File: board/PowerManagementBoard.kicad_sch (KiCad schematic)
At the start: 0 parts

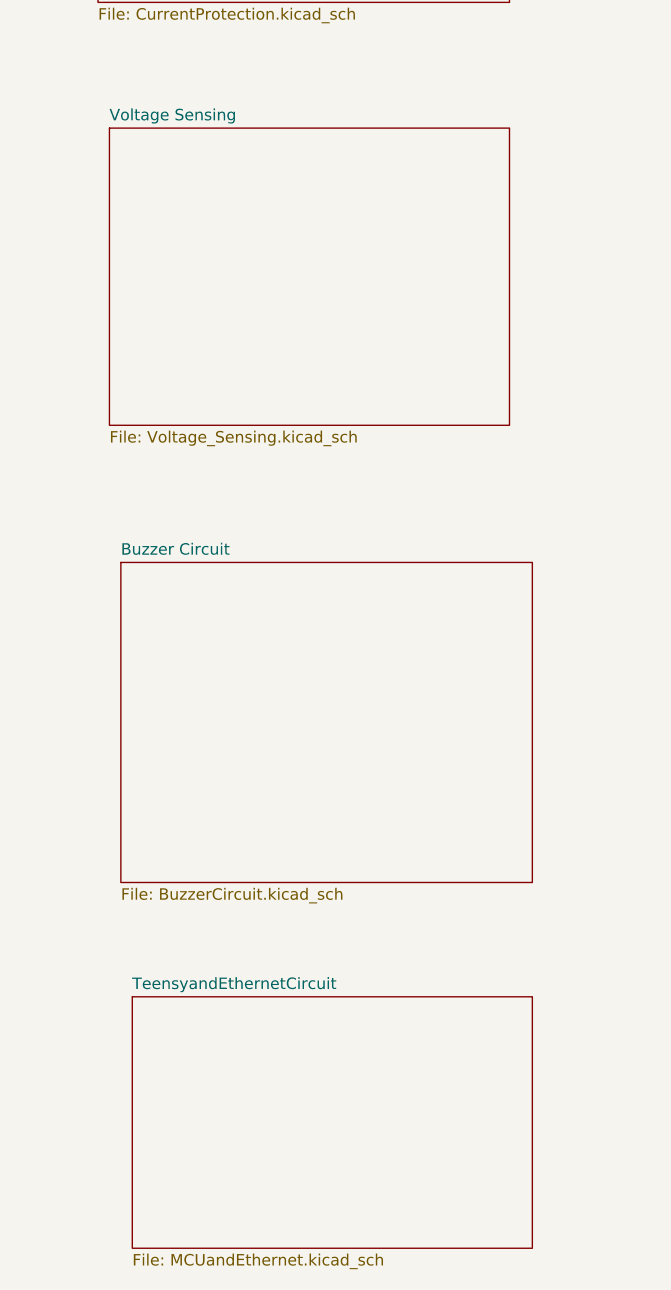
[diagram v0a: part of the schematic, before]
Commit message: added current sense flags to teensy
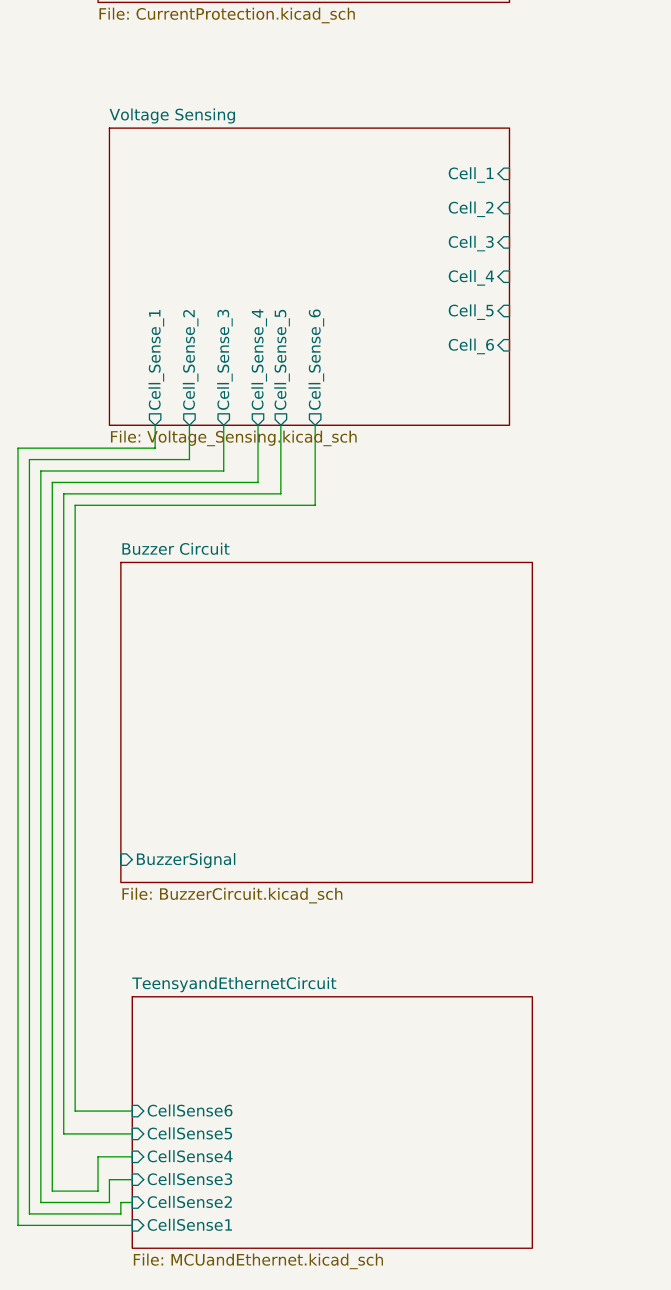
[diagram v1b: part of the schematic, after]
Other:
- sheet Buzzer Circuit ports: added BuzzerSignal; removed none
- sheet TeensyandEthernetCircuit ports: added CellSense1, CellSense2, CellSense3, CellSense4, CellSense5, CellSense6; removed none
- sheet Voltage Sensing ports: added Cell_1, Cell_2, Cell_3, Cell_4, Cell_5, Cell_6, Cell_Sense_1, Cell_Sense_2, Cell_Sense_3, Cell_Sense_4, Cell_Sense_5, Cell_Sense_6; removed none

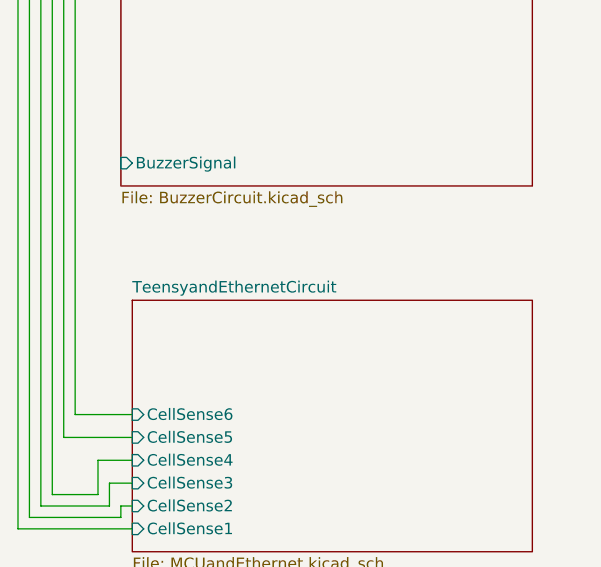
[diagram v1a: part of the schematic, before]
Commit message: Added MCU Flags
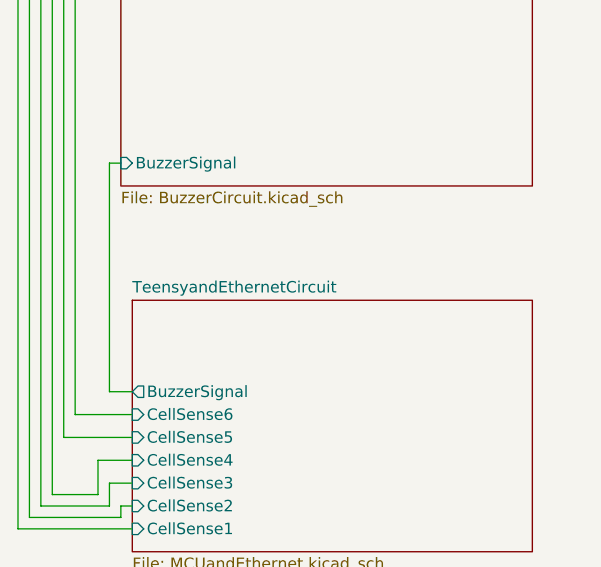
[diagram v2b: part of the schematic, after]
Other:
- sheet TeensyandEthernetCircuit ports: added BuzzerSignal; removed none
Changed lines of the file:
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@@
+	(wire
+		(pts
+			(xy 22.86 179.07) (xy 25.4 179.07)
+		)
+		(stroke
+			(width 0)
+			(type default)
+		)
+	)
 	(wire
 		(pts
@@
 	(wire
 		(pts
+			(xy 22.86 153.67) (xy 22.86 179.07)
+		)
+		(stroke
+			(width 0)
+			(type default)
+		)
+	)
+	(wire
+		(pts
 			(xy 41.91 105.41) (xy 41.91 113.03)
 		)
@@
 		(pts
 			(xy 12.7 107.95) (xy 12.7 194.31)
+		)
+		(stroke
+			(width 0)
+			(type default)
+		)
+	)
+	(wire
+		(pts
+			(xy 24.13 153.67) (xy 22.86 153.67)
 		)
 		(stroke
@@
 			(effects
 				(font
+					(size 1.27 1.27)
+				)
+				(justify left)
+			)
+		)
+		(pin "BuzzerSignal" output
+			(at 25.4 179.07 180)
+			(effects
+				(font

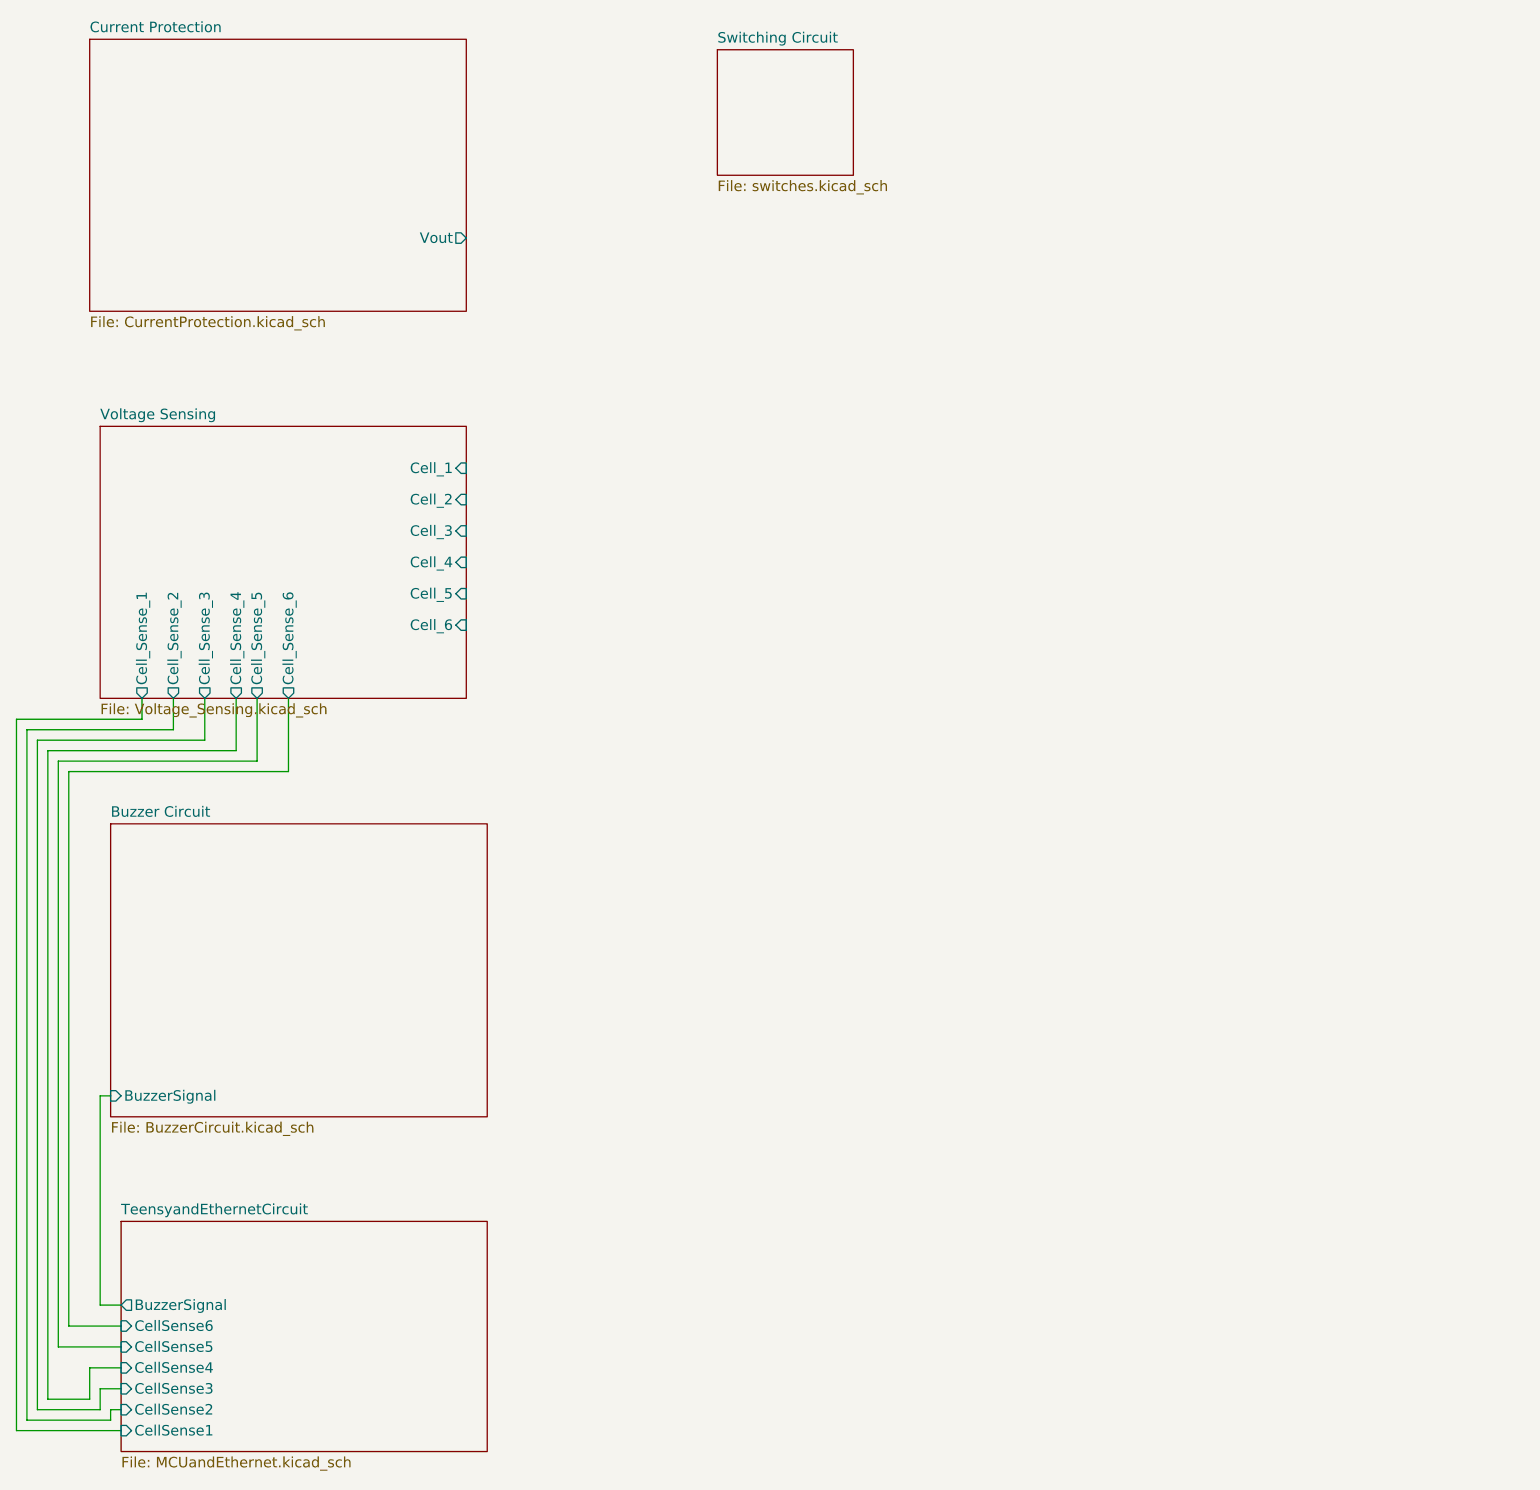
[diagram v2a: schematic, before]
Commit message: added wiring and Voltage Sense Fix
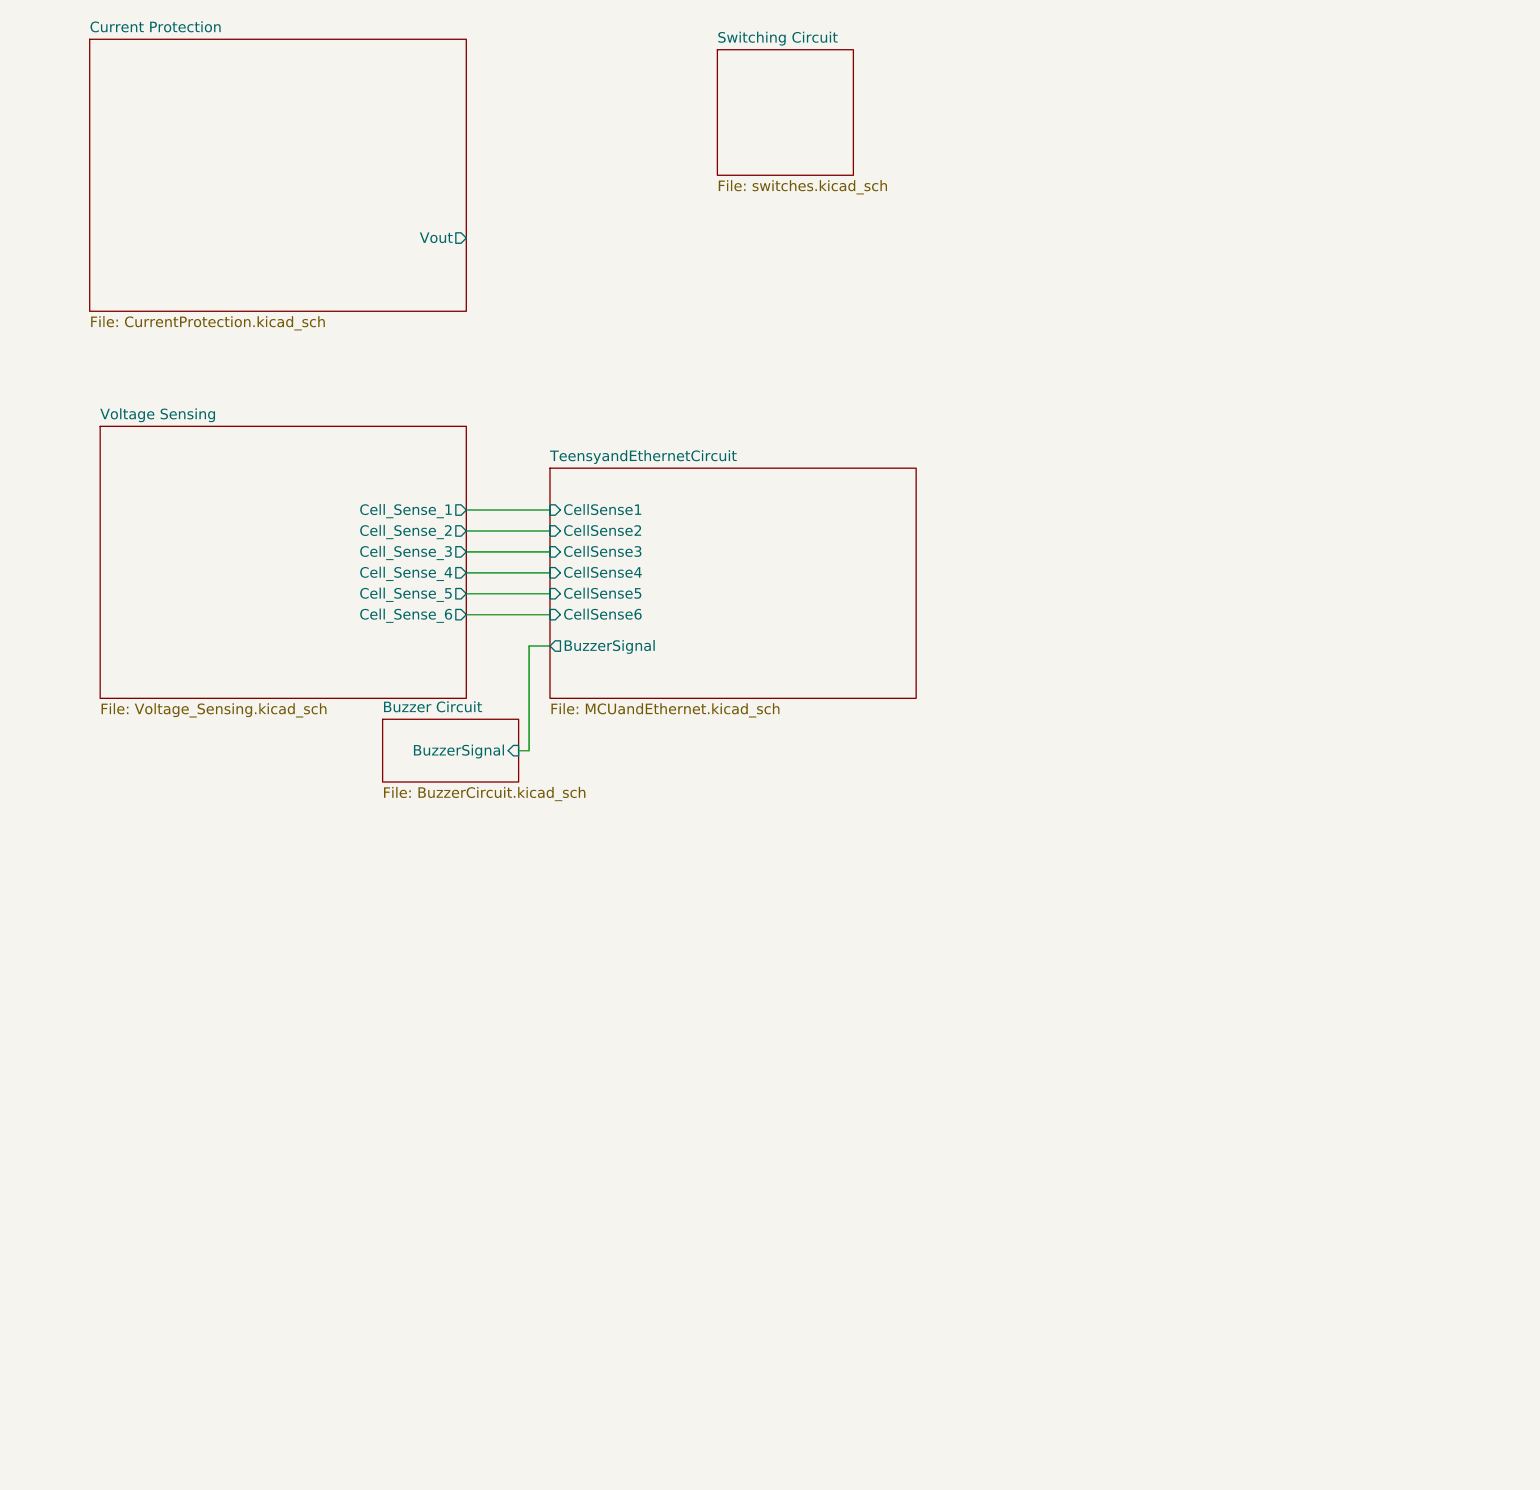
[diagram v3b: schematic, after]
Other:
- sheet Voltage Sensing ports: added none; removed Cell_1, Cell_2, Cell_3, Cell_4, Cell_5, Cell_6

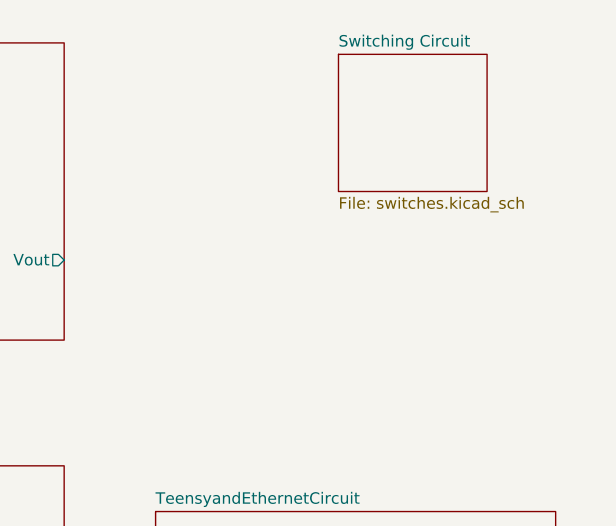
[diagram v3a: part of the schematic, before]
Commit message: add POE
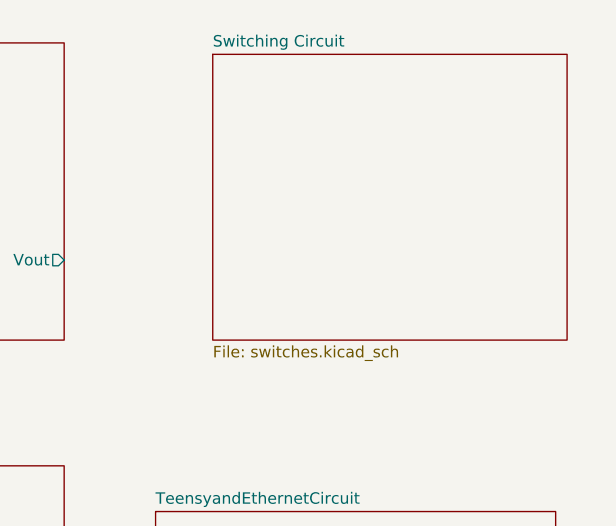
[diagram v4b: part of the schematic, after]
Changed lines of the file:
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@@
 	)
 	(sheet
-		(at 97.79 26.67)
-		(size 16.51 15.24)
+		(at 83.82 26.67)
+		(size 39.37 31.75)
 		(exclude_from_sim no)
 		(in_bom yes)
@@
 		)
 		(property "Sheetname" "Switching Circuit"
-			(at 97.79 25.9584 0)
+			(at 83.82 25.9584 0)
 			(effects
 				(font
@@
 		)
 		(property "Sheetfile" "switches.kicad_sch"
-			(at 97.79 42.4946 0)
+			(at 83.82 59.0046 0)
 			(effects
 				(font

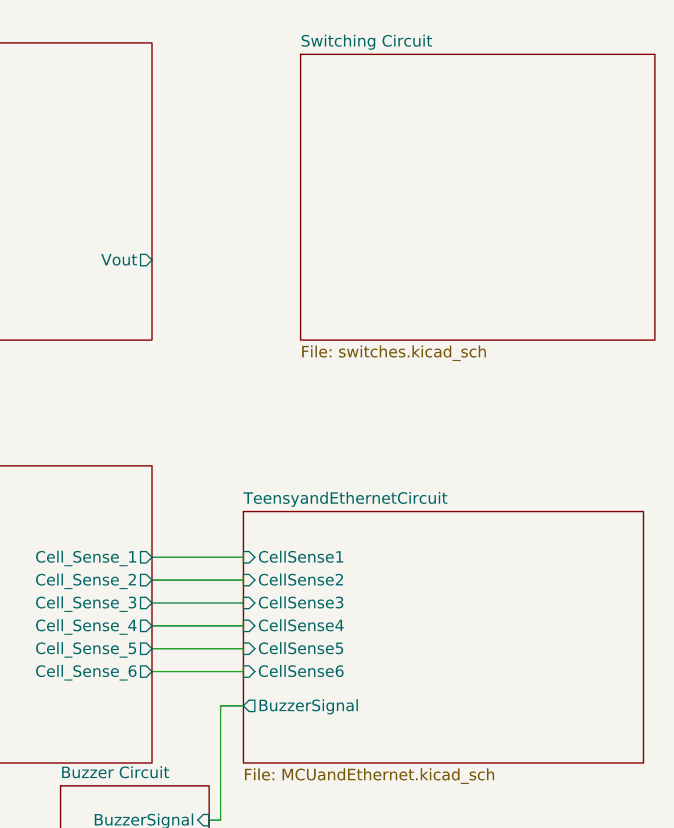
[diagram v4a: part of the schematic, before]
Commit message: add mosfett and teensy switch pins
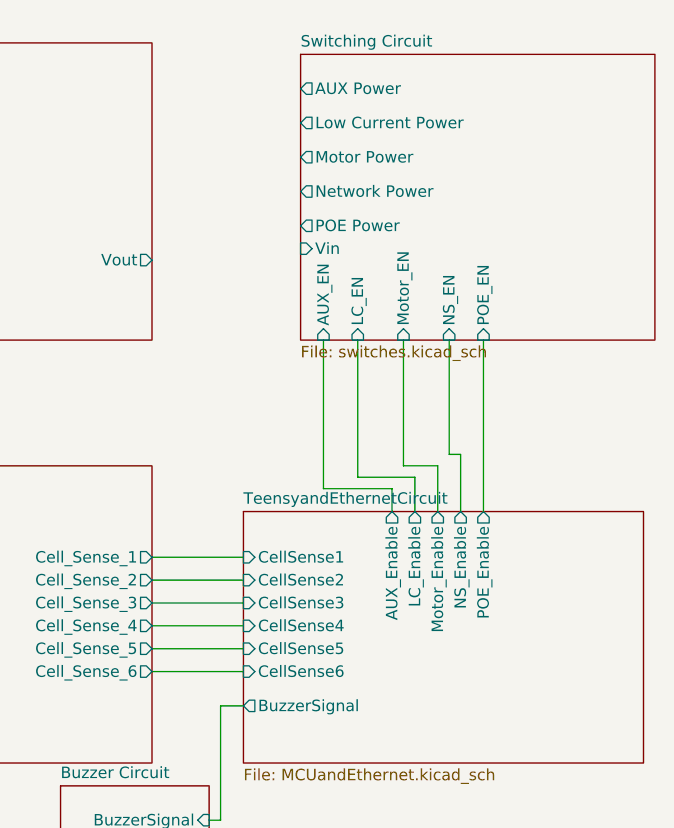
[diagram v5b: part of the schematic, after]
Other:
- sheet Switching Circuit ports: added AUX Power, AUX_EN, LC_EN, Low Current Power, Motor Power, Motor_EN, NS_EN, Network Power, POE Power, POE_EN, Vin; removed none
- sheet TeensyandEthernetCircuit ports: added AUX_Enable, LC_Enable, Motor_Enable, NS_Enable, POE_Enable; removed none
